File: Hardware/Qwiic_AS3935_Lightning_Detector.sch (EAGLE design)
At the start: 30 parts, among them U1 AS3935

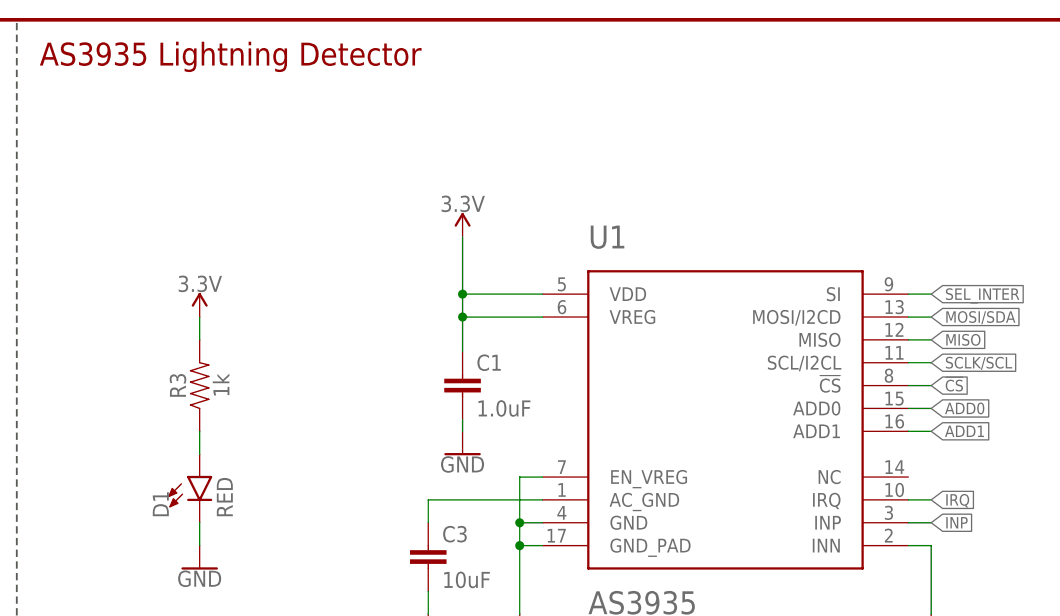
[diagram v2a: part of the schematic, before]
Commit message: Fixes clearance issues after changing DRC to SparkFun-tight.drc, Adds disconnect jumper to power LED
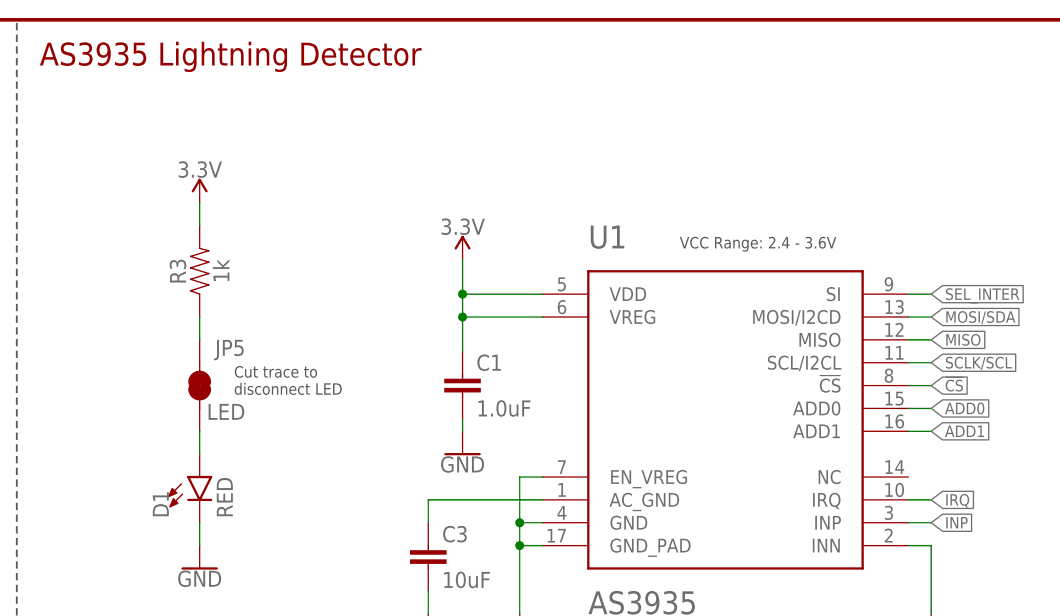
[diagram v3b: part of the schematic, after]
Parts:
- added JP5: LED, SparkFun-Jumpers:JUMPER-SMT_2_NC_TRACE_SILK
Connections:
- new net N$5: D1.A, JP5.1
- net N$1: now also JP5.2; no longer D1.A
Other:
- note added: "Cut trace to disconnect LED"
- note added: "VCC Range: 2.4 - 3.6V"
- moved on the sheet: R3
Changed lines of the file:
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@@
 <part name="LOGO3" library="SparkFun-Aesthetics" deviceset="SFE_LOGO_FLAME" device=".1_INCH"/>
 <part name="H2" library="SparkFun-Hardware" deviceset="STAND-OFF" device="TIGHT"/>
+<part name="JP5" library="SparkFun-Jumpers" deviceset="JUMPER-SMT_2_NC_TRACE" device="_SILK" value="LED"/>
 </parts>
 <sheets>
@@
 <wire x1="30.48" y1="114.3" x2="35.56" y2="114.3" width="0.2032" layer="97" style="shortdash"/>
 <wire x1="45.72" y1="114.3" x2="48.26" y2="114.3" width="0.2032" layer="97" style="shortdash"/>
+<text x="185.42" y="160.02" size="1.27" layer="97">VCC Range: 2.4 - 3.6V</text>
+<text x="135.89" y="143.764" size="1.27" layer="97" font="vector">Cut trace to
+disconnect LED</text>
 </plain>
 <instances>
@@
 <attribute name="VALUE" x="64.516" y="148.59" size="1.778" layer="96" font="vector" rot="R270" align="top-center"/>
 </instance>
-<instance part="SUPPLY1" gate="G$1" x="161.29" y="161.29" smashed="yes">
-<attribute name="VALUE" x="161.29" y="164.084" size="1.778" layer="96" align="bottom-center"/>
+<instance part="SUPPLY1" gate="G$1" x="161.29" y="158.75" smashed="yes">
+<attribute name="VALUE" x="161.29" y="161.544" size="1.778" layer="96" align="bottom-center"/>
 </instance>
 <instance part="GND1" gate="1" x="167.64" y="116.84" smashed="yes">
@@
 <attribute name="VALUE" x="133.985" y="130.048" size="1.778" layer="96" font="vector" rot="R90" align="top-left"/>
 </instance>
-<instance part="R3" gate="G$1" x="132.08" y="144.78" smashed="yes" rot="R90">
-<attribute name="NAME" x="130.556" y="144.78" size="1.778" layer="95" font="vector" rot="R90" align="bottom-center"/>
-<attribute name="VALUE" x="133.604" y="144.78" size="1.778" layer="96" font="vector" rot="R90" align="top-center"/>
-</instance>
-<instance part="SUPPLY6" gate="G$1" x="132.08" y="152.4" smashed="yes">
-<attribute name="VALUE" x="132.08" y="155.194" size="1.778" layer="96" align="bottom-center"/>
+<instance part="R3" gate="G$1" x="132.08" y="157.48" smashed="yes" rot="R90">
+<attribute name="NAME" x="130.556" y="157.48" size="1.778" layer="95" font="vector" rot="R90" align="bottom-center"/>
+<attribute name="VALUE" x="133.604" y="157.48" size="1.778" layer="96" font="vector" rot="R90" align="top-center"/>
+</instance>
+<instance part="SUPPLY6" gate="G$1" x="132.08" y="165.1" smashed="yes">
+<attribute name="VALUE" x="132.08" y="167.894" size="1.778" layer="96" align="bottom-center"/>
 </instance>
 <instance part="GND4" gate="1" x="132.08" y="124.46" smashed="yes">
@@
 <instance part="LOGO3" gate="G$1" x="213.36" y="45.72" smashed="yes"/>
 <instance part="H2" gate="G$1" x="236.22" y="17.78" smashed="yes"/>
+<instance part="JP5" gate="G$1" x="132.08" y="144.78" smashed="yes" rot="R90">
+<attribute name="NAME" x="137.16" y="149.86" size="1.778" layer="95" font="vector" rot="R180"/>
+<attribute name="VALUE" x="137.16" y="140.97" size="1.778" layer="96" font="vector" rot="R180" align="top-left"/>
+</instance>
 </instances>
 <busses>
@@
 <junction x="161.29" y="152.4"/>
 <pinref part="SUPPLY1" gate="G$1" pin="3.3V"/>
-<wire x1="161.29" y1="161.29" x2="161.29" y2="154.94" width="0.1524" layer="91"/>
+<wire x1="161.29" y1="158.75" x2="161.29" y2="154.94" width="0.1524" layer="91"/>
 <junction x="161.29" y="154.94"/>
 <pinref part="U1" gate="G$1" pin="VDD"/>
@@
 <segment>
 <pinref part="R3" gate="G$1" pin="2"/>
-<wire x1="132.08" y1="149.86" x2="132.08" y2="152.4" width="0.1524" layer="91"/>
+<wire x1="132.08" y1="162.56" x2="132.08" y2="165.1" width="0.1524" layer="91"/>
 <pinref part="SUPPLY6" gate="G$1" pin="3.3V"/>
 </segment>
@@
 <label x="213.36" y="139.7" size="1.27" layer="95" font="vector" xref="yes"/>
 <pinref part="U1" gate="G$1" pin="ADD1"/>
-</segment>
-</net>
-<net name="N$1" class="0">
-<segment>
-<pinref part="D1" gate="G$1" pin="A"/>
-<pinref part="R3" gate="G$1" pin="1"/>
-<wire x1="132.08" y1="137.16" x2="132.08" y2="139.7" width="0.1524" layer="91"/>
 </segment>
 </net>
@@
 </segment>
 </net>
+<net name="N$1" class="0">
+<segment>
+<pinref part="R3" gate="G$1" pin="1"/>
+<pinref part="JP5" gate="G$1" pin="2"/>
+<wire x1="132.08" y1="152.4" x2="132.08" y2="149.86" width="0.1524" layer="91"/>
+</segment>
+</net>
+<net name="N$5" class="0">
+<segment>
+<pinref part="JP5" gate="G$1" pin="1"/>
+<pinref part="D1" gate="G$1" pin="A"/>
+<wire x1="132.08" y1="139.7" x2="132.08" y2="137.16" width="0.1524" layer="91"/>
+</segment>
+</net>
